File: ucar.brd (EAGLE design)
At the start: 100 x 100 mm, 46 parts, among them IC1 L298, T1 2SC1815, T2 2SC1815

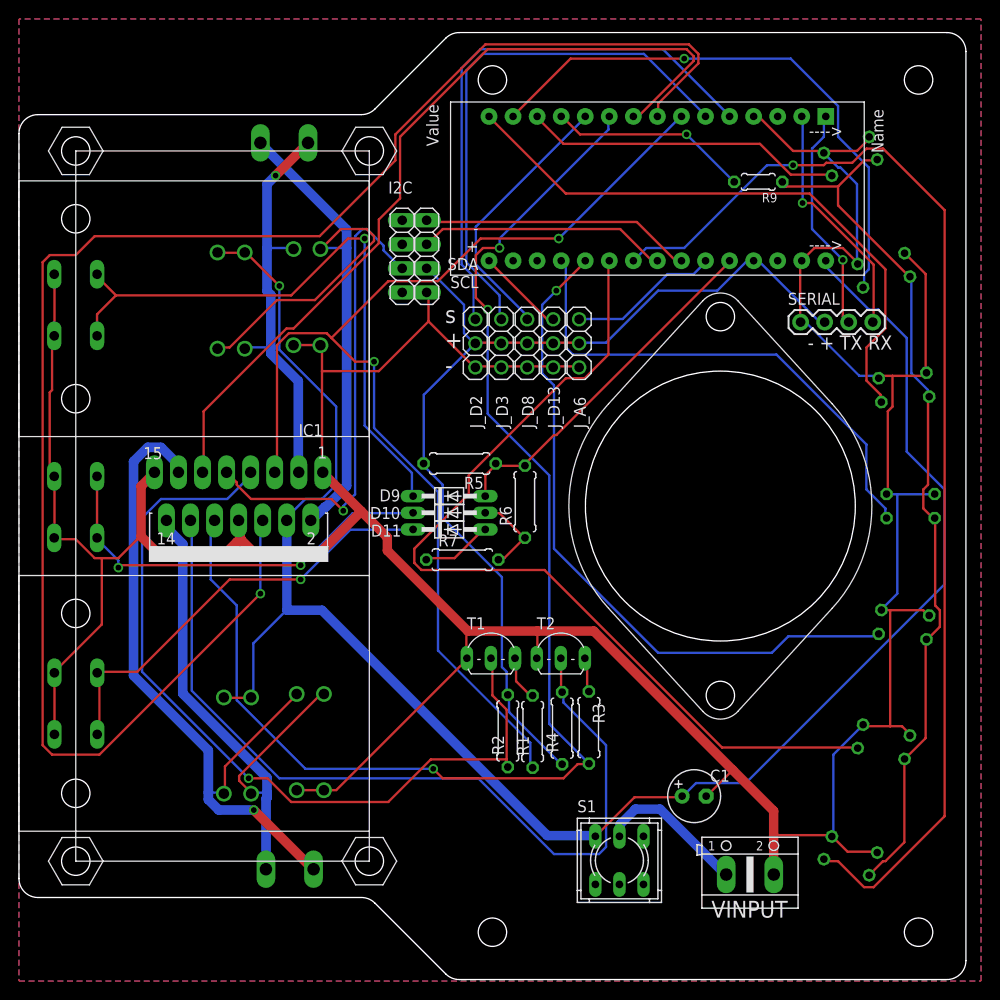
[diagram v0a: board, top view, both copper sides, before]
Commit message: tamiya version
using Tamiya 70093 gearbox for the car
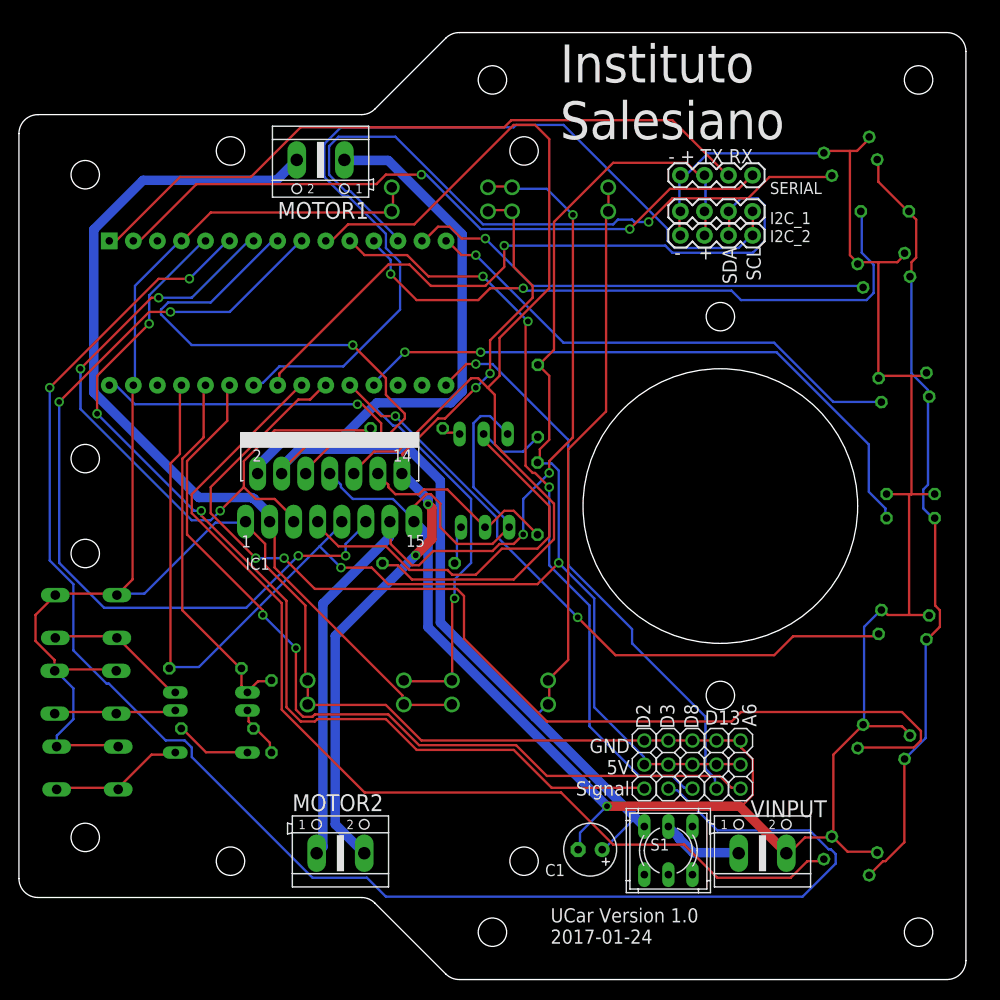
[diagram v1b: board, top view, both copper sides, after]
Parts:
- I2C_1, I2C_2: value (none) -> 1X4-BIG; device pinhead:1X04 -> adafruit:1X04-BIG
- R1, R3: value 10k -> 1k
- R2, R4: value 4.7k -> 10k
- moved U$1 81.8 mm to (7.00, 68.0), flipped to the bottom
- moved D3 68.8 mm to (57.1, 73.7), turned to 0 degrees
- moved D4 65.2 mm to (57.1, 71.1), turned to 0 degrees
- moved D7 60.5 mm to (44.5, 73.7), turned to 0 degrees
- moved D8 57.4 mm to (44.5, 71.1), turned to 0 degrees
- moved D2 50.5 mm to (50.8, 19.1), turned to 0 degrees
- moved D1 50.0 mm to (50.8, 21.6), turned to 0 degrees
- moved J_D2 47.9 mm to (66.0, 12.7), turned to 270 degrees
- moved J_D3 47.9 mm to (68.6, 12.7), turned to 270 degrees
- moved J_D8 47.8 mm to (71.1, 12.7), turned to 270 degrees
- moved J_D13 47.7 mm to (73.7, 12.7), turned to 270 degrees
- moved J_A6 47.6 mm to (76.2, 12.7), turned to 270 degrees
- moved D6 43.5 mm to (35.6, 19.1), turned to 0 degrees
- moved D5 40.6 mm to (35.6, 21.6), turned to 0 degrees
- moved R6 35.1 mm to (26.7, 17.8), flipped to the bottom
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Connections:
- net N$11 renamed TX
- net N$17 renamed RX
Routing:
- net E1: track 178.5 -> 60.6 mm
- net D3: track 56.7 -> 169.0 mm, vias 0 -> 2
- net A6: track 16.0 -> 91.6 mm, vias 0 -> 2
- net N$9: track 91.1 -> 21.7 mm
- net SCL: track 31.3 -> 95.1 mm
- net D8: track 28.5 -> 81.7 mm, vias 0 -> 3
- net N$5: track 43.6 -> 96.6 mm, vias 1 -> 0
- net D13: track 9.34 -> 60.5 mm, vias 0 -> 1
- net N$14: track 66.2 -> 15.3 mm, vias 1 -> 0
- net TX: track 24.0 -> 73.1 mm, vias 1 -> 0
- net GND: track 404.1 -> 452.7 mm, vias 0 -> 1
- net RX: track 25.5 -> 73.0 mm, vias 1 -> 2
- net LED: track 21.1 -> 67.2 mm, vias 1 -> 2
- net M1: track 122.1 -> 76.5 mm, vias 2 -> 3
- net D2: track 59.3 -> 104.4 mm, vias 0 -> 3
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- removed copper zone on layer 16, net N$18
- removed copper zone on layer 1, net N$19
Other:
- outline, holes or cut-outs redrawn
- board text added: "+"
- board text added: "-"
- board text added: "A6"
- board text added: "D13"
- board text added: "D2"
- board text added: "D3"
- board text added: "D8"
- board text added: "GND 5V Signal"
- board text added: "Instituto Salesiano"
- board text added: "SCL"
- board text added: "SDA"
- board text added: "UCar Version 1.0 2017-01-24"
- board text removed: "+ -"
- board text removed: "- +"
- board text removed: "- + SDA SCL"
- board text removed: "---->"
- board text removed: "I2C"
- board text removed: "s + -"
